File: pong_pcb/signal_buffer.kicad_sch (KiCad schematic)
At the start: 10 parts, among them U4 SN74LVC2G34DBV, U5 74LVC2G34, U6 74LVC2G34, U7 74LVC2G34, U8 74LVC2G34

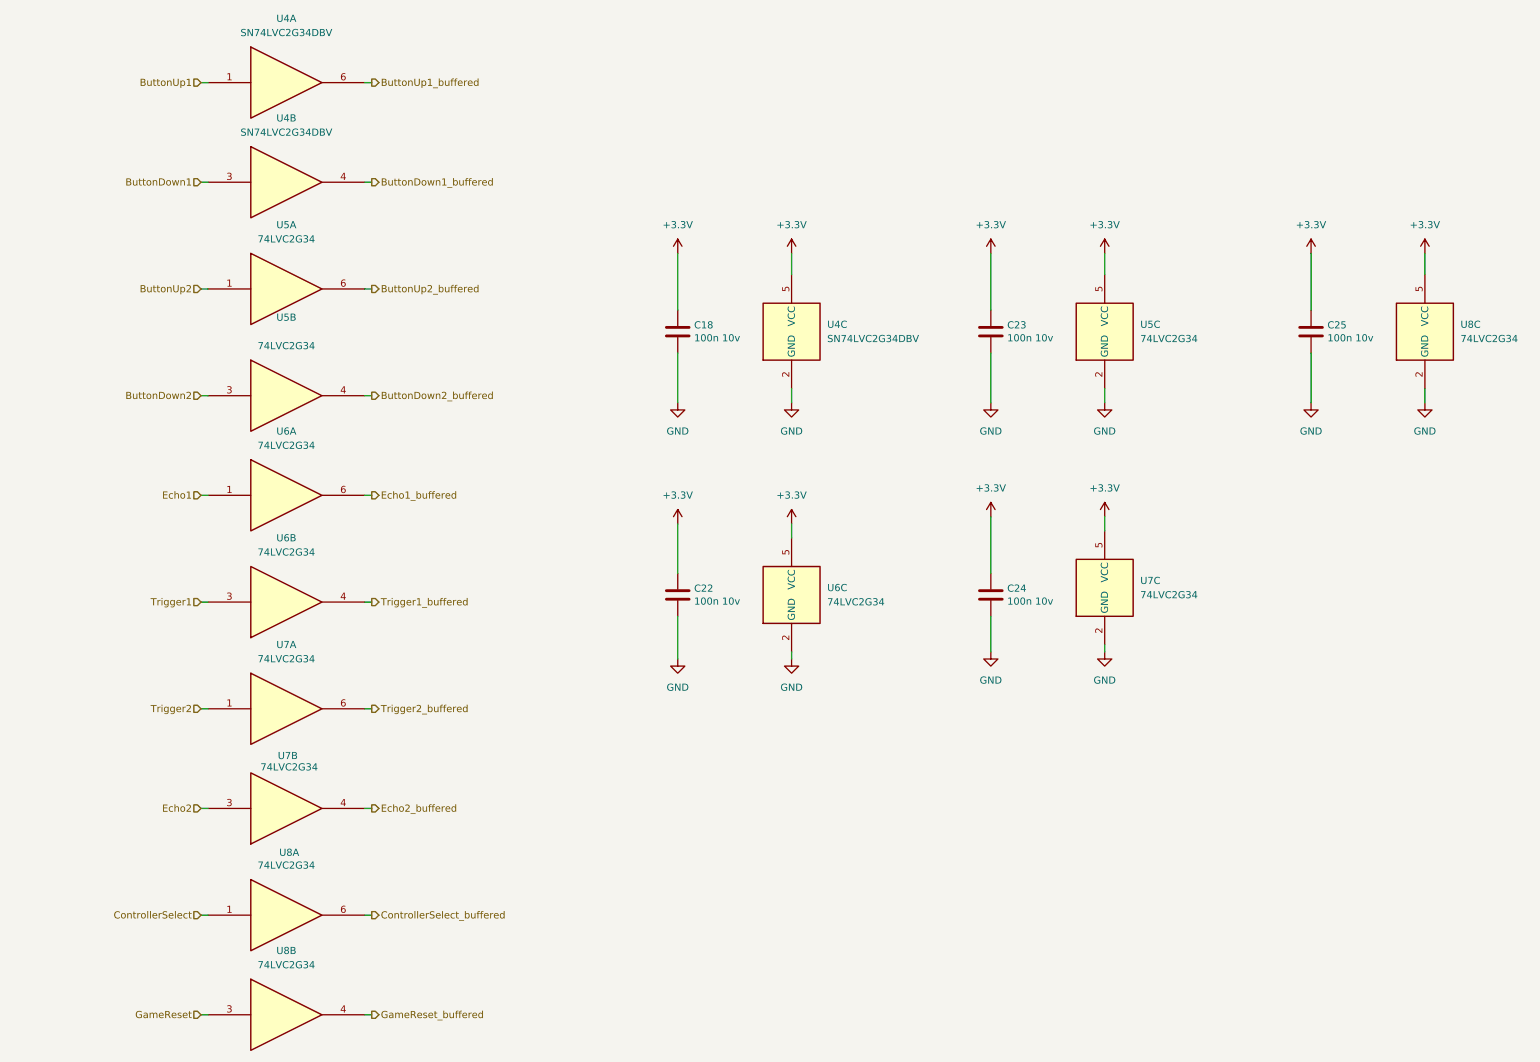
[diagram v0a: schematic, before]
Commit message: Update schema and add packages
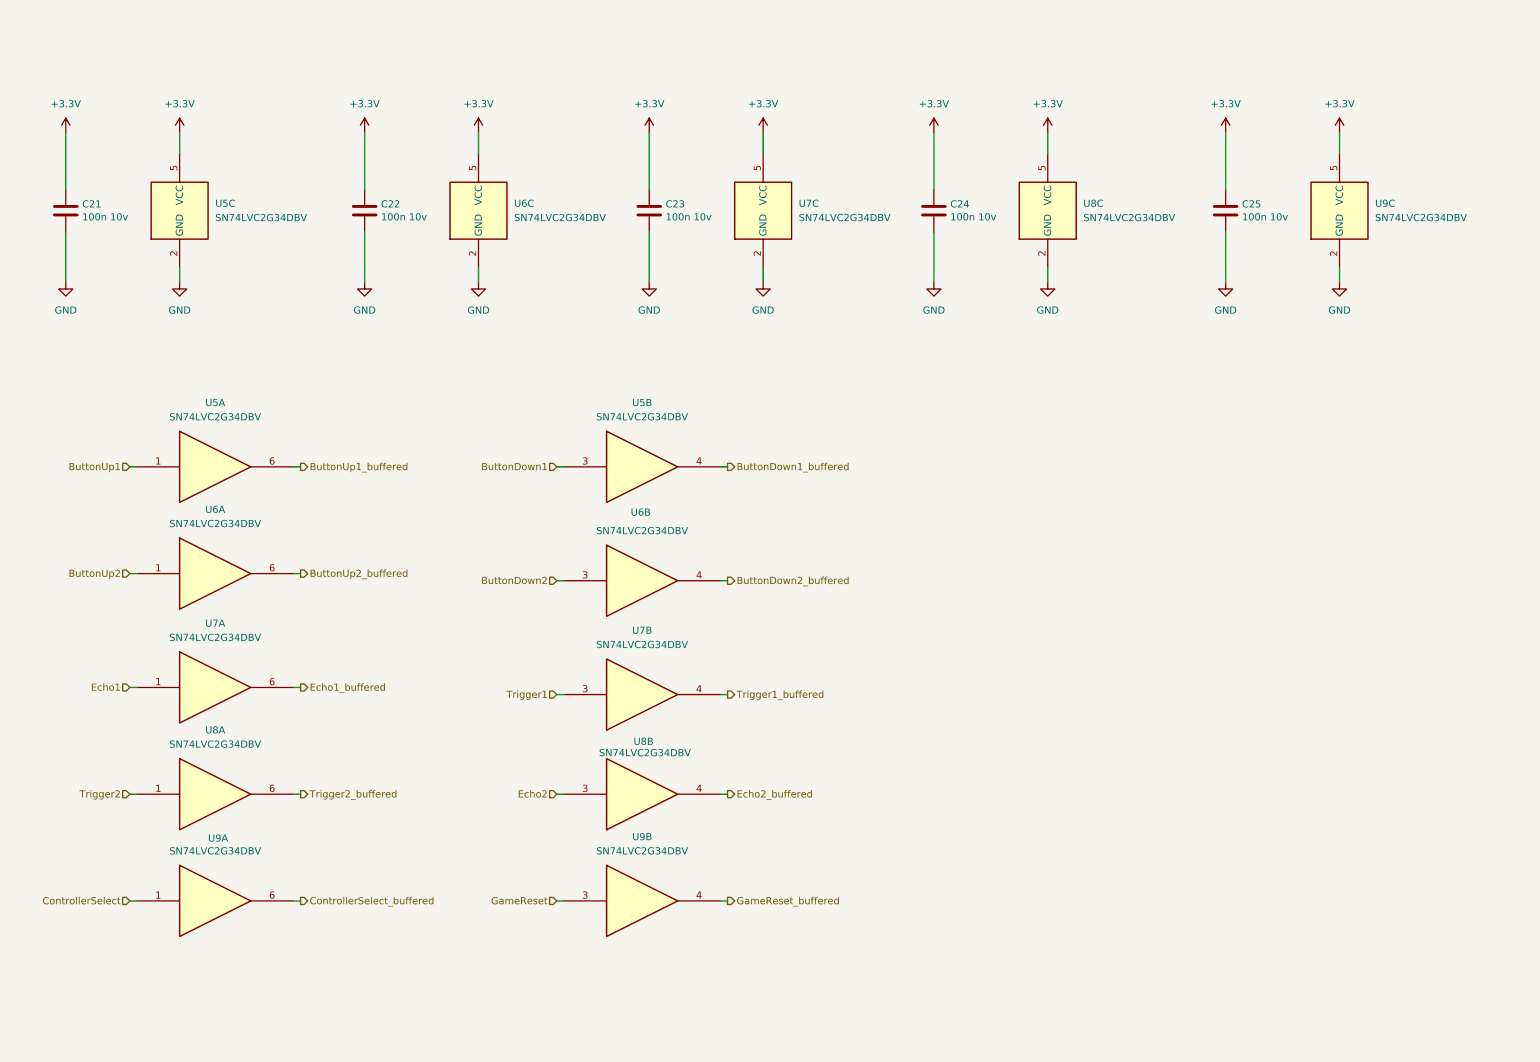
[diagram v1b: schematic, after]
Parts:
- U5: renamed from U4; footprint Package_TO_SOT_SMD:SOT-23-6 -> Package_TO_SOT_SMD:SOT-23-6_Handsoldering
- U6: renamed from U5; value 74LVC2G34 -> SN74LVC2G34DBV; footprint (none) -> Package_TO_SOT_SMD:SOT-23-6_Handsoldering
- U7, U8: renamed from U6; value 74LVC2G34 -> SN74LVC2G34DBV; footprint (none) -> Package_TO_SOT_SMD:SOT-23-6_Handsoldering
- U7, U9: renamed from U8; value 74LVC2G34 -> SN74LVC2G34DBV; footprint (none) -> Package_TO_SOT_SMD:SOT-23-6_Handsoldering
- U8, U9: renamed from U7; value 74LVC2G34 -> SN74LVC2G34DBV; footprint (none) -> Package_TO_SOT_SMD:SOT-23-6_Handsoldering
- renumbered C18 to C21, C23 to C22, C25 to C23, C22 to C24, C24 to C25
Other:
- company: (none) -> Fontys
- title: (none) -> Signal buffers
- moved on the sheet: C21, C22, C23, C24, C25, U5A, U5B, U5C, U6A, U6B, U6C, U7A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

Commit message: Add HDMI layout
And others
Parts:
- C21, C22, C23, C24, C25: footprint Capacitor_SMD:C_0402_1005Metric_Pad0.74x0.62mm_HandSolder -> Capacitor_SMD:C_0603_1608Metric
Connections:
- net Echo2: now also U8.1; no longer U8.3
- net Echo2_buffered: now also U8.6; no longer U8.4
- net Trigger2: now also U8.3; no longer U8.1
- net Trigger2_buffered: now also U8.4; no longer U8.6

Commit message: Update schema and route PCB
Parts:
- renumbered C21 to C27, C22 to C28, C23 to C29, C24 to C30, C25 to C31
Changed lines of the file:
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@@
 		(on_board yes)
 		(dnp no)
-		(property "Reference" "C24"
+		(property "Reference" "C30"
 			(at 187.071 44.5516 0)
 			(effects
@@
 			(project "pong_pcb"
 				(path "/676c80a8-0f91-4e34-b1e8-b545e51bb5da/eac229f5-8d83-41ab-ad2e-d2bc0cddb3f4"
-					(reference "C24")
+					(reference "C30")
 					(unit 1)
 				)
@@
 		(dnp no)
 		(fields_autoplaced yes)
-		(property "Reference" "#PWR091"
+		(property "Reference" "#PWR0106"
 			(at 236.22 64.77 0)
 			(effects
@@
 			(project "pong_pcb"
 				(path "/676c80a8-0f91-4e34-b1e8-b545e51bb5da/eac229f5-8d83-41ab-ad2e-d2bc0cddb3f4"
-					(reference "#PWR091")
+					(reference "#PWR0106")
 					(unit 1)
 				)
@@
 		(dnp no)
 		(fields_autoplaced yes)
-		(property "Reference" "#PWR077"
+		(property "Reference" "#PWR092"
 			(at 133.35 35.56 0)
 			(effects
@@
 			(project "pong_pcb"
 				(path "/676c80a8-0f91-4e34-b1e8-b545e51bb5da/eac229f5-8d83-41ab-ad2e-d2bc0cddb3f4"
-					(reference "#PWR077")
+					(reference "#PWR092")
 					(unit 1)
 				)
@@
 		(on_board yes)
 		(dnp no)
-		(property "Reference" "C25"
+		(property "Reference" "C31"
 			(at 239.141 44.5516 0)
 			(effects
@@
 			(project "pong_pcb"
 				(path "/676c80a8-0f91-4e34-b1e8-b545e51bb5da/eac229f5-8d83-41ab-ad2e-d2bc0cddb3f4"
-					(reference "C25")
+					(reference "C31")
 					(unit 1)
 				)
@@
 		(dnp no)
 		(fields_autoplaced yes)
-		(property "Reference" "#PWR087"
+		(property "Reference" "#PWR0102"
 			(at 133.35 64.77 0)
 			(effects
@@
 			(project "pong_pcb"
 				(path "/676c80a8-0f91-4e34-b1e8-b545e51bb5da/eac229f5-8d83-41ab-ad2e-d2bc0cddb3f4"
-					(reference "#PWR087")
+					(reference "#PWR0102")
 					(unit 1)
 				)
@@
 		(dnp no)
 		(fields_autoplaced yes)
-		(property "Reference" "#PWR078"
+		(property "Reference" "#PWR093"
 			(at 153.67 35.56 0)
 			(effects
@@
 			(project "pong_pcb"
 				(path "/676c80a8-0f91-4e34-b1e8-b545e51bb5da/eac229f5-8d83-41ab-ad2e-d2bc0cddb3f4"
-					(reference "#PWR078")
+					(reference "#PWR093")
 					(unit 1)
 				)
@@
 		(dnp no)
 		(fields_autoplaced yes)
-		(property "Reference" "#PWR086"
+		(property "Reference" "#PWR0101"
 			(at 102.87 64.77 0)
 			(effects
@@
 			(project "pong_pcb"
 				(path "/676c80a8-0f91-4e34-b1e8-b545e51bb5da/eac229f5-8d83-41ab-ad2e-d2bc0cddb3f4"
-					(reference "#PWR086")
+					(reference "#PWR0101")
 					(unit 1)
 				)
@@
 		(dnp no)
 		(fields_autoplaced yes)
-		(property "Reference" "#PWR088"
+		(property "Reference" "#PWR0103"
 			(at 153.67 64.77 0)
 			(effects
@@
 			(project "pong_pcb"
 				(path "/676c80a8-0f91-4e34-b1e8-b545e51bb5da/eac229f5-8d83-41ab-ad2e-d2bc0cddb3f4"
-					(reference "#PWR088")
+					(reference "#PWR0103")
 					(unit 1)
 				)
@@
 		(dnp no)
 		(fields_autoplaced yes)
-		(property "Reference" "#PWR081"
+		(property "Reference" "#PWR096"
 			(at 236.22 35.56 0)
 			(effects
@@
 			(project "pong_pcb"
 				(path "/676c80a8-0f91-4e34-b1e8-b545e51bb5da/eac229f5-8d83-41ab-ad2e-d2bc0cddb3f4"
-					(reference "#PWR081")
+					(reference "#PWR096")
 					(unit 1)
 				)
@@
 		(dnp no)
 		(fields_autoplaced yes)
-		(property "Reference" "#PWR092"
+		(property "Reference" "#PWR0107"
 			(at 256.54 64.77 0)
 			(effects
@@
 			(project "pong_pcb"
 				(path "/676c80a8-0f91-4e34-b1e8-b545e51bb5da/eac229f5-8d83-41ab-ad2e-d2bc0cddb3f4"
-					(reference "#PWR092")
+					(reference "#PWR0107")
 					(unit 1)
 				)
@@
 		(on_board yes)
 		(dnp no)
-		(property "Reference" "C23"
+		(property "Reference" "C29"
 			(at 136.271 44.5516 0)
 			(effects
@@
 			(project "pong_pcb"
 				(path "/676c80a8-0f91-4e34-b1e8-b545e51bb5da/eac229f5-8d83-41ab-ad2e-d2bc0cddb3f4"
-					(reference "C23")
+					(reference "C29")
 					(unit 1)
 				)
@@
 		(dnp no)
 		(fields_autoplaced yes)
-		(property "Reference" "#PWR073"
+		(property "Reference" "#PWR088"
 			(at 29.21 35.56 0)
 			(effects
@@
 			(project "pong_pcb"
 				(path "/676c80a8-0f91-4e34-b1e8-b545e51bb5da/eac229f5-8d83-41ab-ad2e-d2bc0cddb3f4"
-					(reference "#PWR073")
+					(reference "#PWR088")
 					(unit 1)
 				)
@@
 		(dnp no)
 		(fields_autoplaced yes)
-		(property "Reference" "#PWR085"
+		(property "Reference" "#PWR0100"
 			(at 82.55 64.77 0)
 			(effects
@@
 			(project "pong_pcb"
 				(path "/676c80a8-0f91-4e34-b1e8-b545e51bb5da/eac229f5-8d83-41ab-ad2e-d2bc0cddb3f4"
-					(reference "#PWR085")
+					(reference "#PWR0100")
 					(unit 1)
 				)
@@
 		(on_board yes)
 		(dnp no)
-		(property "Reference" "C21"
+		(property "Reference" "C27"
 			(at 32.131 44.5516 0)
 			(effects
@@
 			(project "pong_pcb"
 				(path "/676c80a8-0f91-4e34-b1e8-b545e51bb5da/eac229f5-8d83-41ab-ad2e-d2bc0cddb3f4"
-					(reference "C21")
+					(reference "C27")
 					(unit 1)
 				)
@@
 		(on_board yes)
 		(dnp no)
-		(property "Reference" "C22"
+		(property "Reference" "C28"
 			(at 85.471 44.5516 0)
 			(effects
@@
 			(project "pong_pcb"
 				(path "/676c80a8-0f91-4e34-b1e8-b545e51bb5da/eac229f5-8d83-41ab-ad2e-d2bc0cddb3f4"
-					(reference "C22")
+					(reference "C28")
 					(unit 1)
 				)
@@
 		(dnp no)
 		(fields_autoplaced yes)
-		(property "Reference" "#PWR083"
+		(property "Reference" "#PWR098"
 			(at 29.21 64.77 0)
 			(effects
@@
 			(project "pong_pcb"
 				(path "/676c80a8-0f91-4e34-b1e8-b545e51bb5da/eac229f5-8d83-41ab-ad2e-d2bc0cddb3f4"
-					(reference "#PWR083")
+					(reference "#PWR098")
 					(unit 1)
 				)
@@
 		(dnp no)
 		(fields_autoplaced yes)
-		(property "Reference" "#PWR076"
+		(property "Reference" "#PWR091"
 			(at 102.87 35.56 0)
 			(effects
@@
 			(project "pong_pcb"
 				(path "/676c80a8-0f91-4e34-b1e8-b545e51bb5da/eac229f5-8d83-41ab-ad2e-d2bc0cddb3f4"
-					(reference "#PWR076")
+					(reference "#PWR091")
 					(unit 1)
 				)
@@
 		(dnp no)
 		(fields_autoplaced yes)
-		(property "Reference" "#PWR082"
+		(property "Reference" "#PWR097"
 			(at 256.54 35.56 0)
 			(effects
@@
 			(project "pong_pcb"
 				(path "/676c80a8-0f91-4e34-b1e8-b545e51bb5da/eac229f5-8d83-41ab-ad2e-d2bc0cddb3f4"
-					(reference "#PWR082")
+					(reference "#PWR097")
 					(unit 1)
 				)
@@
 		(dnp no)
 		(fields_autoplaced yes)
-		(property "Reference" "#PWR080"
+		(property "Reference" "#PWR095"
 			(at 204.47 35.56 0)
 			(effects
@@
 			(project "pong_pcb"
 				(path "/676c80a8-0f91-4e34-b1e8-b545e51bb5da/eac229f5-8d83-41ab-ad2e-d2bc0cddb3f4"
-					(reference "#PWR080")
+					(reference "#PWR095")
 					(unit 1)
 				)
@@
 		(dnp no)
 		(fields_autoplaced yes)
-		(property "Reference" "#PWR075"
+		(property "Reference" "#PWR090"
 			(at 82.55 35.56 0)
 			(effects
@@
 			(project "pong_pcb"
 				(path "/676c80a8-0f91-4e34-b1e8-b545e51bb5da/eac229f5-8d83-41ab-ad2e-d2bc0cddb3f4"
-					(reference "#PWR075")
+					(reference "#PWR090")
 					(unit 1)
 				)
@@
 		(dnp no)
 		(fields_autoplaced yes)
-		(property "Reference" "#PWR084"
+		(property "Reference" "#PWR099"
 			(at 49.53 64.77 0)
 			(effects
@@
 			(project "pong_pcb"
 				(path "/676c80a8-0f91-4e34-b1e8-b545e51bb5da/eac229f5-8d83-41ab-ad2e-d2bc0cddb3f4"
-					(reference "#PWR084")
+					(reference "#PWR099")
 					(unit 1)
 				)
@@
 		(dnp no)
 		(fields_autoplaced yes)
-		(property "Reference" "#PWR089"
+		(property "Reference" "#PWR0104"
 			(at 184.15 64.77 0)
 			(effects
@@
 			(project "pong_pcb"
 				(path "/676c80a8-0f91-4e34-b1e8-b545e51bb5da/eac229f5-8d83-41ab-ad2e-d2bc0cddb3f4"
-					(reference "#PWR089")
+					(reference "#PWR0104")
 					(unit 1)
 				)
@@
 		(dnp no)
 		(fields_autoplaced yes)
-		(property "Reference" "#PWR074"
+		(property "Reference" "#PWR089"
 			(at 49.53 35.56 0)
 			(effects
@@
 			(project "pong_pcb"
 				(path "/676c80a8-0f91-4e34-b1e8-b545e51bb5da/eac229f5-8d83-41ab-ad2e-d2bc0cddb3f4"
-					(reference "#PWR074")
+					(reference "#PWR089")
 					(unit 1)
 				)
@@
 		(dnp no)
 		(fields_autoplaced yes)
-		(property "Reference" "#PWR090"
+		(property "Reference" "#PWR0105"
 			(at 204.47 64.77 0)
 			(effects
@@
 			(project "pong_pcb"
 				(path "/676c80a8-0f91-4e34-b1e8-b545e51bb5da/eac229f5-8d83-41ab-ad2e-d2bc0cddb3f4"
-					(reference "#PWR090")
+					(reference "#PWR0105")
 					(unit 1)
 				)
@@
 		(dnp no)
 		(fields_autoplaced yes)
-		(property "Reference" "#PWR079"
+		(property "Reference" "#PWR094"
 			(at 184.15 35.56 0)
 			(effects
@@
 			(project "pong_pcb"
 				(path "/676c80a8-0f91-4e34-b1e8-b545e51bb5da/eac229f5-8d83-41ab-ad2e-d2bc0cddb3f4"
-					(reference "#PWR079")
-					(unit 1)
-				)
+					(reference "#PWR094")
+					(unit 1)
+				)
